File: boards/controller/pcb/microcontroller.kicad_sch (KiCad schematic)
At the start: 21 parts, among them SW3001 SW_Push, SW3002 SW_Push, U3001 STM32U575VITx, X3001 16MHz

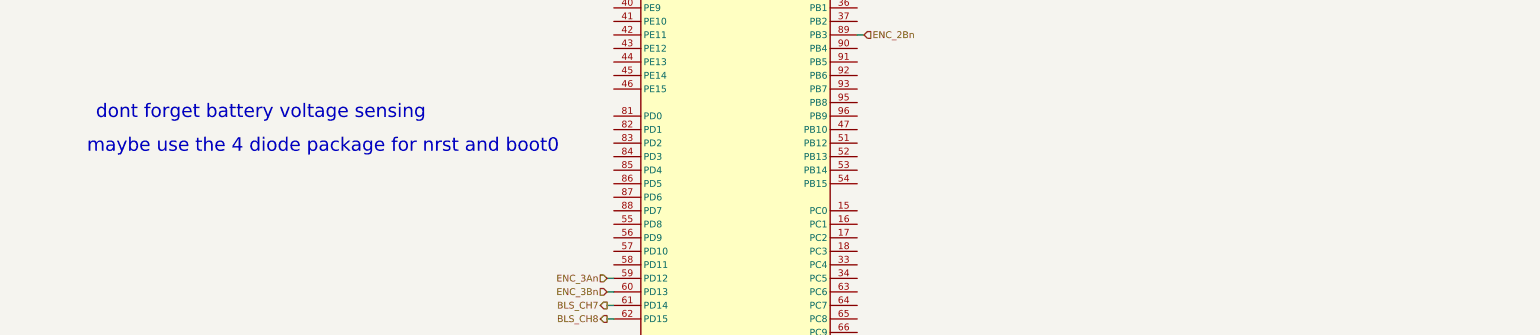
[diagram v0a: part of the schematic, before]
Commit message: controller: pcb: Update schematic notes
Signed-off-by: Nicholas Loehrke <nicholasnloehrke@gmail.com>
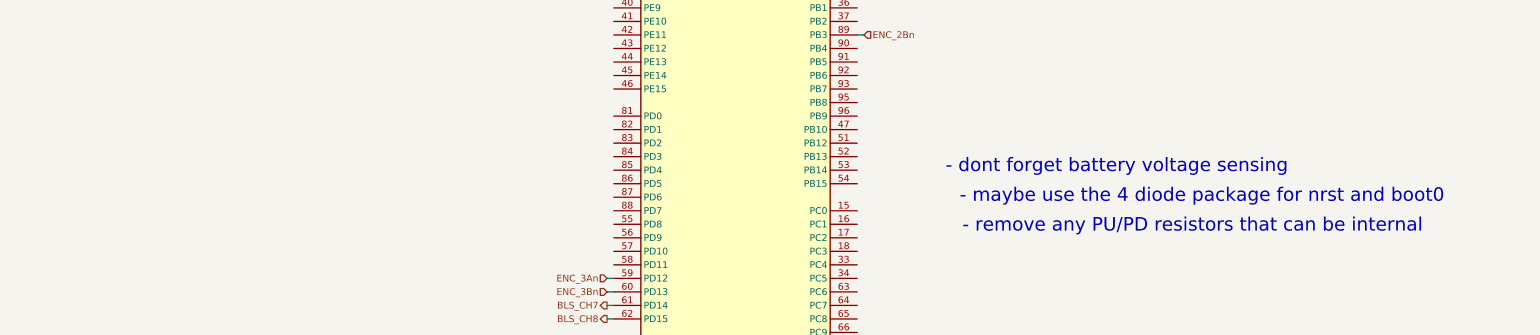
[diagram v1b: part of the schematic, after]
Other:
- note added: "- dont forget battery voltage sensing"
- note added: "- maybe use the 4 diode package for nrst and boot0"
- note added: "- remove any PU/PD resistors that can be internal"
- note removed: "dont forget battery voltage sensing"
- note removed: "maybe use the 4 diode package for nrst and boot0"
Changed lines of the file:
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@@
 		)
 	)
-	(text "maybe use the 4 diode package for nrst and boot0"
+	(text "- maybe use the 4 diode package for nrst and boot0"
 		(exclude_from_sim no)
-		(at 63.5 113.538 0)
+		(at 228.6 122.936 0)
+		(effects
+			(font
+				(size 2.54 2.54)
+			)
+		)
+	)
+	(text "- remove any PU/PD resistors that can be internal"
+		(exclude_from_sim no)
+		(at 226.822 128.524 0)
 		(effects
 			(font
@@
 		)
 	)
-	(text "dont forget battery voltage sensing"
+	(text "- dont forget battery voltage sensing"
 		(exclude_from_sim no)
-		(at 51.816 107.188 0)
+		(at 212.598 117.348 0)
 		(effects
 			(font

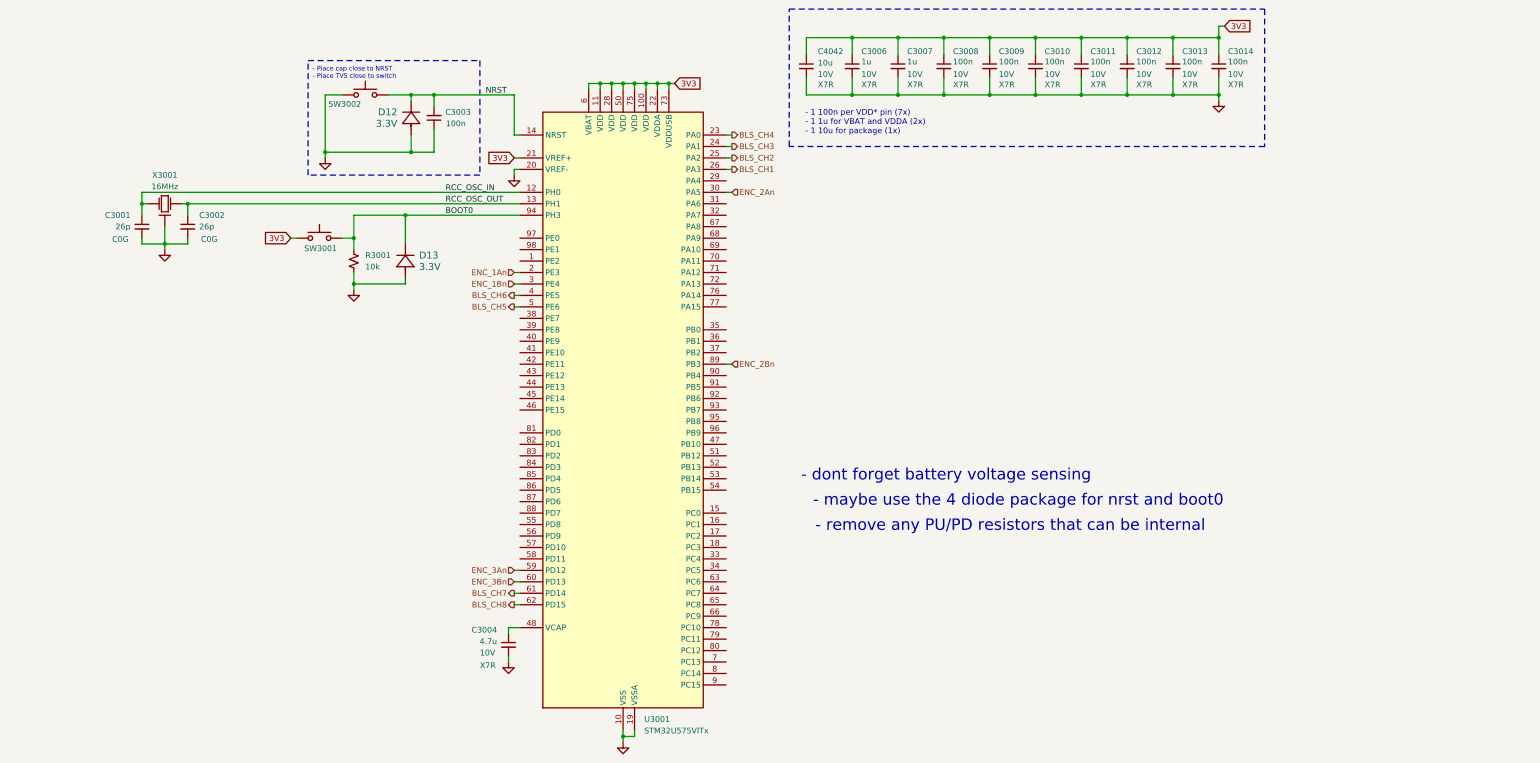
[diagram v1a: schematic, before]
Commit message: controller: pcb: Update schematic
Signed-off-by: Nicholas Loehrke <nicholasnloehrke@gmail.com>
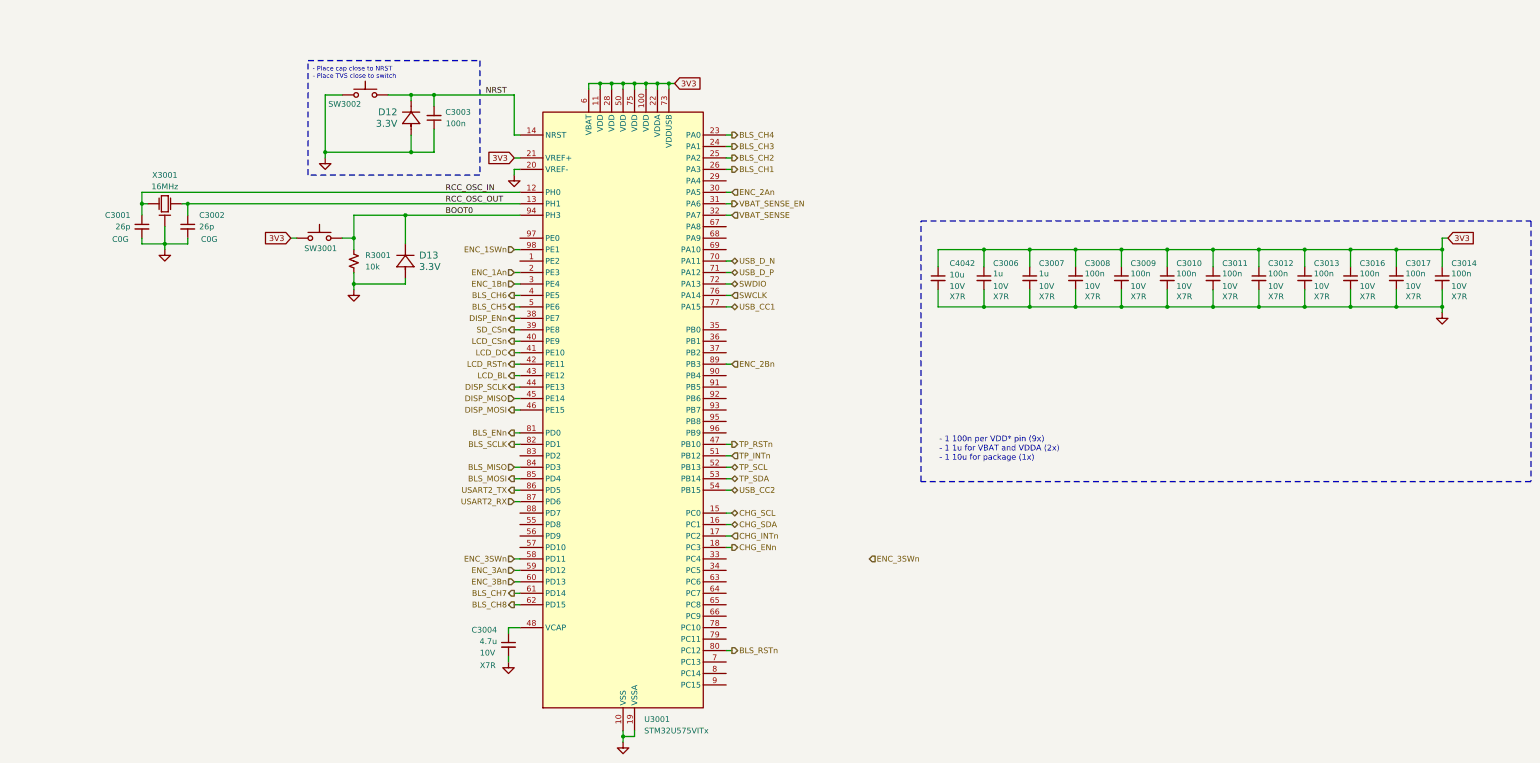
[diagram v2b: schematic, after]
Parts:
- added C3016, C3017: 100n, symbol Device:C_Small
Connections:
- net 3V3: now also C3016.1, C3017.1
- net GND: now also C3016.2, C3017.2
- net CHG_SCL: now reaches U3001.15 (PC0)
- net CHG_SDA: now reaches U3001.16 (PC1)
- net CHG_INTn: now reaches U3001.17 (PC2)
- net CHG_ENn: now reaches U3001.18 (PC3)
- net VBAT_SENSE_EN: now reaches U3001.31 (PA6)
- net VBAT_SENSE: now reaches U3001.32 (PA7)
- net DISP_ENn: now reaches U3001.38 (PE7)
- net SD_CSn: now reaches U3001.39 (PE8)
- net LCD_CSn: now reaches U3001.40 (PE9)
- net LCD_DC: now reaches U3001.41 (PE10)
- net LCD_RSTn: now reaches U3001.42 (PE11)
- net LCD_BL: now reaches U3001.43 (PE12)
- net DISP_SCLK: now reaches U3001.44 (PE13)
- net DISP_MISO: now reaches U3001.45 (PE14)
- net DISP_MOSI: now reaches U3001.46 (PE15)
- net TP_RSTn: now reaches U3001.47 (PB10)
- net TP_INTn: now reaches U3001.51 (PB12)
- net TP_SCL: now reaches U3001.52 (PB13)
- net TP_SDA: now reaches U3001.53 (PB14)
- net USB_CC2: now reaches U3001.54 (PB15)
- net ENC_3SWn: now reaches U3001.58 (PD11)
- net USB_D_N: now reaches U3001.70 (PA11)
- net USB_D_P: now reaches U3001.71 (PA12)
- net SWDIO: now reaches U3001.72 (PA13)
- net SWCLK: now reaches U3001.76 (PA14)
- net USB_CC1: now reaches U3001.77 (PA15)
- net BLS_RSTn: now reaches U3001.80 (PC12)
- net BLS_ENn: now reaches U3001.81 (PD0)
- net BLS_SCLK: now reaches U3001.82 (PD1)
- net BLS_MISO: now reaches U3001.84 (PD3)
- net BLS_MOSI: now reaches U3001.85 (PD4)
- net USART2_TX: now reaches U3001.86 (PD5)
- net USART2_RX: now reaches U3001.87 (PD6)
- net ENC_1SWn: now reaches U3001.98 (PE1)
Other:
- note added: "- 1 100n per VDD* pin (9x) - 1 1u for VBAT and VDDA (2x) - 1 10u for package (1x)"
- note removed: "- 1 100n per VDD* pin (7x) - 1 1u for VBAT and VDDA (2x) - 1 10u for package (1x)"
- note removed: "- dont forget battery voltage sensing"
- note removed: "- maybe use the 4 diode package for nrst and boot0"
- note removed: "- remove any PU/PD resistors that can be internal"
- moved on the sheet: C3006, C3007, C3008, C3009, C3010, C3011, C3012, C3013, C3014, C4042

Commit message: controller: pcb: Update schematic + layout
Signed-off-by: Nicholas Loehrke <nicholasnloehrke@gmail.com>
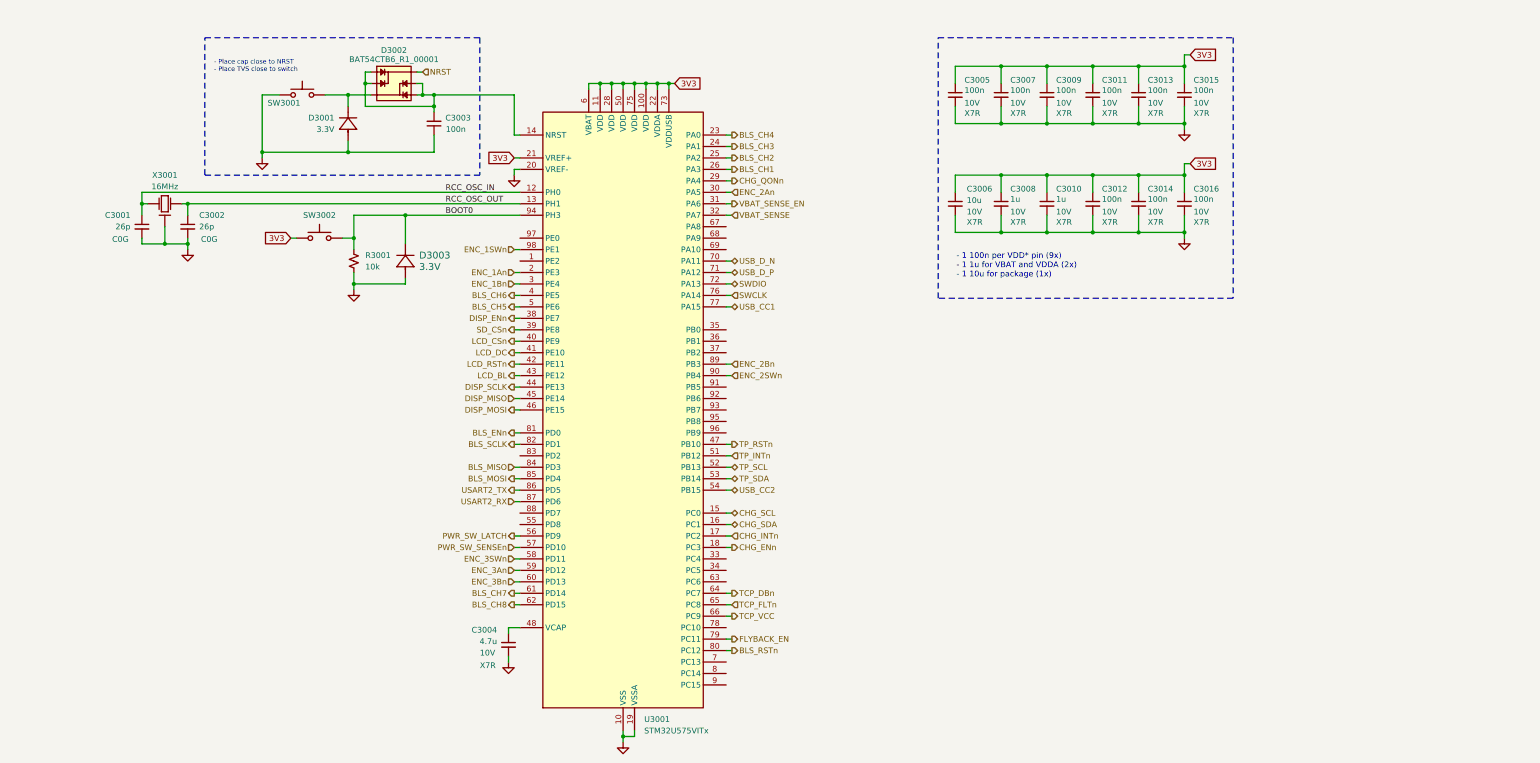
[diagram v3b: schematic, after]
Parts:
- removed SW3001, SW3002: SW_Push, symbol Switch:SW_Push
- added D3002: ~, Package_TO_SOT_SMD:SOT-563, symbol BAT54CTB6_R1_00001:BAT54CTB6_R1_00001
- added SW3001, SW3002: PTS526 SK15 SMTR2 LFS, PTS526_SK15_SMTR2_LFS:PTS526_SK15_SMTR2_LFS, symbol PTS526_SK15_SMTR2_LFS:PTS526_SK15_SMTR2_LFS
- C3001, C3002, C3003: footprint (none) -> Capacitor_SMD:C_0402_1005Metric
- C3004: footprint (none) -> Capacitor_SMD:C_0805_2012Metric
- C3005: renamed from C3011; footprint (none) -> Capacitor_SMD:C_0402_1005Metric
- C3006: renamed from C4042; footprint (none) -> Capacitor_SMD:C_1210_3225Metric
- C3007: renamed from C3012; footprint (none) -> Capacitor_SMD:C_0402_1005Metric
- C3008: renamed from C3006; footprint (none) -> Capacitor_SMD:C_0603_1608Metric
- C3009: renamed from C3013; footprint (none) -> Capacitor_SMD:C_0402_1005Metric
- C3010: renamed from C3007; footprint (none) -> Capacitor_SMD:C_0603_1608Metric
- C3011: renamed from C3016; footprint (none) -> Capacitor_SMD:C_0402_1005Metric
- C3012: renamed from C3008; footprint (none) -> Capacitor_SMD:C_0402_1005Metric
- C3013: renamed from C3017; footprint (none) -> Capacitor_SMD:C_0402_1005Metric
- C3014: renamed from C3009; footprint (none) -> Capacitor_SMD:C_0402_1005Metric
- C3015: renamed from C3014; footprint (none) -> Capacitor_SMD:C_0402_1005Metric
- C3016: renamed from C3010; footprint (none) -> Capacitor_SMD:C_0402_1005Metric
- D3001: renamed from D12; footprint CR_SOD-523_PNJ -> PJSD03TS-AU_R1_000A1:PJSD03TS-AU_R1_000A1
- D3003: renamed from D13; footprint CR_SOD-523_PNJ -> PJSD03TS-AU_R1_000A1:PJSD03TS-AU_R1_000A1
- R3001: footprint (none) -> Resistor_SMD:R_0402_1005Metric
- X3001: footprint RH100-16.000-18-2030-EXT-TR_RAL -> RH100-16.000-18-2030-EXT-TR:RH100-16.000-18-2030-EXT-TR
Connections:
- net 3V3: now also SW3002.1, SW3002.2
- net BOOT0: now also SW3002.3, SW3002.4
- net GND: now also SW3001.1, SW3001.2
- net NRST: now also D3002.6; no longer C3003.2, D3001.1, U3001.14 (NRST)
- net CHG_QONn: now reaches U3001.29 (PA4)
- net PWR_SW_LATCH: now reaches U3001.56 (PD9)
- net PWR_SW_SENSEn: now reaches U3001.57 (PD10)
- net TCP_DBn: now reaches U3001.64 (PC7)
- net TCP_FLTn: now reaches U3001.65 (PC8)
- net TCP_VCC: now reaches U3001.66 (PC9)
- net FLYBACK_EN: now reaches U3001.79 (PC11)
- net ENC_2SWn: now reaches U3001.90 (PB4)
- new net: C3003.2, D3002.1, D3002.2, D3002.4, D3002.5, U3001.14 (NRST)
- new net: D3001.1, D3002.3, SW3001.3, SW3001.4
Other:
- moved on the sheet: C3003, C3005, C3006, C3007, C3008, C3009, C3010, C3011, C3012, C3013, C3014, C3015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

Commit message: controller: Update BOM
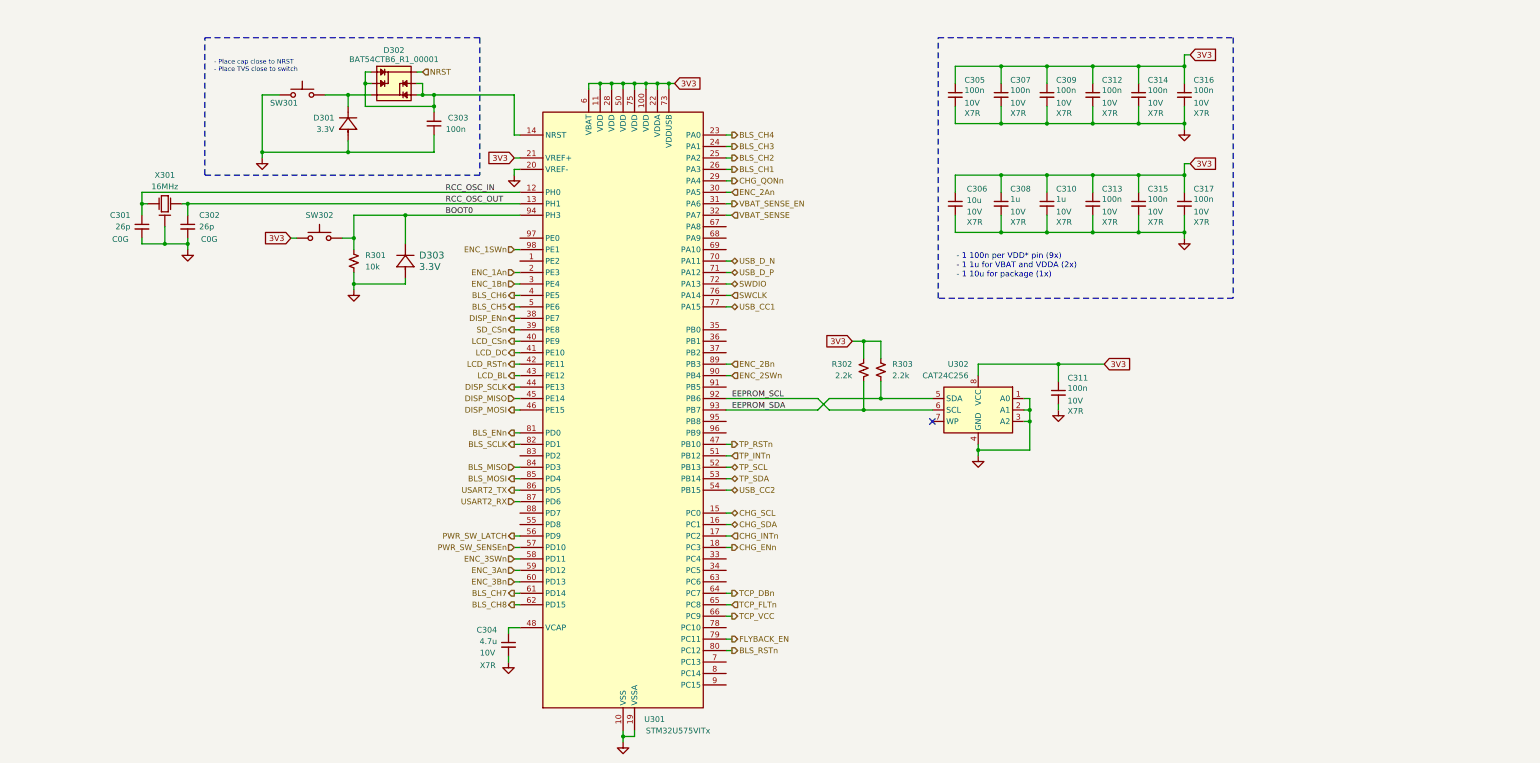
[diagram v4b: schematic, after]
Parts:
- added C311: 100n, Capacitor_SMD:C_0402_1005Metric, symbol Device:C_Small
- added R302, R303: 2.2k, Resistor_SMD:R_0402_1005Metric, symbol Device:R_Small_US
- added U302: CAT24C256, Package_SO:TSSOP-8_4.4x3mm_P0.65mm, symbol Memory_EEPROM:CAT24C256
- D301: renamed from D3001; MPN (none) -> PJSD03TS-AU_R1_000A1
- D303: renamed from D3003; MPN (none) -> PJSD03TS-AU_R1_000A1
- SW301: renamed from SW3001; MPN (none) -> PTS526 SK15 SMTR2 LFS
- SW302: renamed from SW3002; value PTS526 SK15 SMTR2 LFS -> PTS526SK15SMTR2 LFS; MPN (none) -> PTS526SK15SMTR2 LFS
- U301: renamed from U3001; MPN (none) -> STM32U575VITx
- X301: renamed from X3001; MPN (none) -> RH100-16.000-18-2030-EXT-TR
- renumbered C3001 to C301, C3002 to C302, C3003 to C303, C3004 to C304, C3005 to C305, C3006 to C306, C3007 to C307, C3008 to C308, C3009 to C309, C3010 to C310, C3011 to C312, C3012 to C313, C3013 to C314, C3014 to C315, C3015 to C316, C3016 to C317, D3002 to D302, R3001 to R301
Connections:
- net 3V3: now also C311.1, R302.2, R303.2, U302.8 (VCC)
- net GND: now also C311.2, U302.1 (A0), U302.2 (A1), U302.3 (A2), U302.4 (GND)
- net EEPROM_SCL: now reaches U301.92 (PB6)
- net EEPROM_SCL: now also R302.1, U302.6 (SCL)
- net EEPROM_SDA: now reaches U301.93 (PB7)
- net EEPROM_SDA: now also R303.1, U302.5 (SDA)
- no-connect marks 0 -> 1
